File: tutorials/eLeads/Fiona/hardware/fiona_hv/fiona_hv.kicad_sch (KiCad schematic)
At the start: 63 parts, among them J101 MicroFit_VT_4, J102 MicroFit_VT_4, K1 G5Q-1A4-DC5, Q2 SSM3K333R, SW101 SW_SPDT, SW102 SW_SPDT, U101 OpAmp, U102 ATMEGA16M1, U103 OpAmp, U104 LM397, U105 MCP2561-E_SN, U106 AD8494, U107 OpAmp, Y101 Crystal_16MHz_18pF

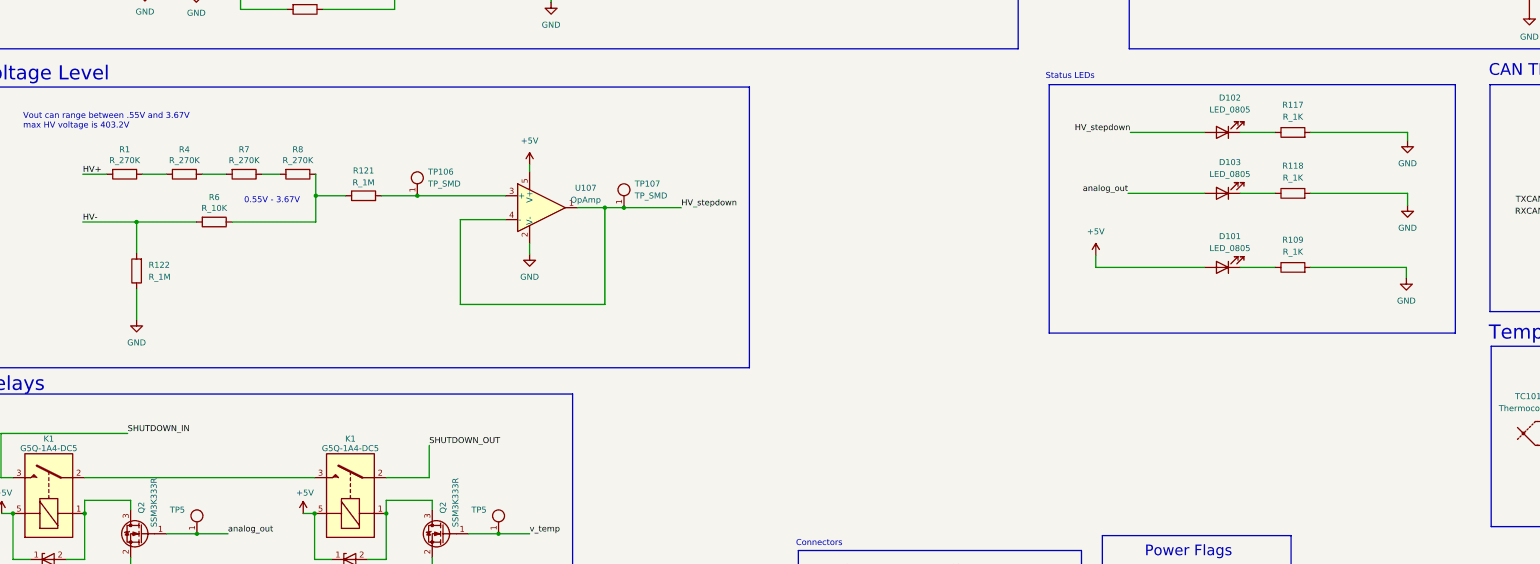
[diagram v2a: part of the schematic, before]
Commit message: Add shutdown LEDs
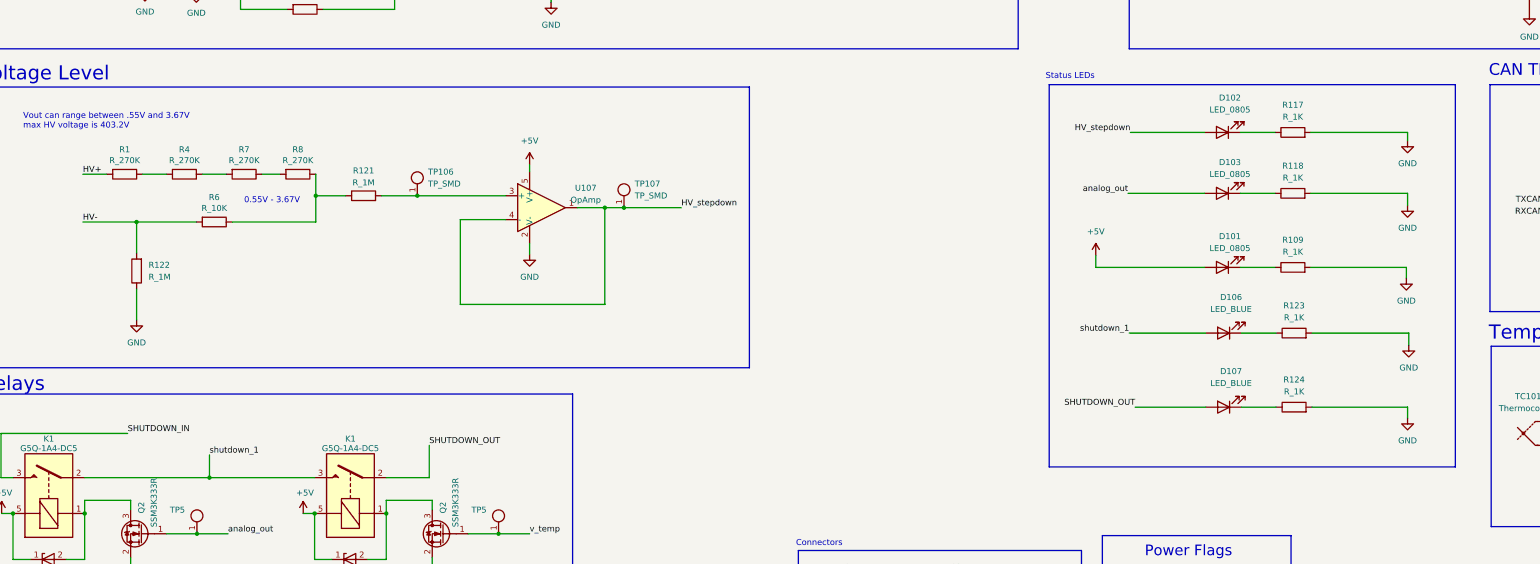
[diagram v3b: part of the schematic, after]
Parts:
- added D106, D107: LED_BLUE, OEM:CHIPLED_0805, symbol OEM:LED_BLUE
- added R123, R124: R_1K, OEM:R_0603, symbol formula:R_1K
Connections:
- net GND: now also R123.2, R124.2
- net SHUTDOWN_OUT: now also D107.2 (A)
- net shutdown_1: now reaches K1.2, K1.3
- net shutdown_1: now also D106.2 (A)
- new net: D106.1 (K), R123.1
- new net: D107.1 (K), R124.1
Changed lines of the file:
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@@
   (junction (at 102.87 41.91) (diameter 0) (color 0 0 0 0)
   )
+  (junction (at 63.754 235.966) (diameter 0) (color 0 0 0 0)
+  )
   (junction (at 277.114 54.61) (diameter 0) (color 0 0 0 0)
   )
@@
     (stroke (width 0) (type default))
   )
+  (wire (pts (xy 283.21 220.98) (xy 290.576 220.98))
+    (stroke (width 0) (type default))
+  )
   (wire (pts (xy 162.814 41.91) (xy 162.814 73.406))
     (stroke (width 0) (type default))
@@
     (stroke (width 0) (type default))
   )
+  (wire (pts (xy 275.59 205.232) (xy 259.334 205.232))
+    (stroke (width 0) (type default))
+  )
   (wire (pts (xy 371.856 215.9) (xy 371.856 218.948))
     (stroke (width 0) (type default))
@@
     (stroke (width 0) (type default))
   )
+  (wire (pts (xy 298.196 205.232) (xy 318.77 205.232))
+    (stroke (width 0) (type default))
+  )
   (wire (pts (xy 46.99 240.792) (xy 46.99 242.824))
     (stroke (width 0) (type default))
@@
     (stroke (width 0) (type default))
   )
+  (wire (pts (xy 63.754 231.14) (xy 63.754 235.966))
+    (stroke (width 0) (type default))
+  )
   (wire (pts (xy 377.952 180.34) (xy 381.762 180.34))
     (stroke (width 0) (type default))
@@
     (stroke (width 0) (type default))
   )
+  (wire (pts (xy 63.754 235.966) (xy 86.106 235.966))
+    (stroke (width 0) (type default))
+  )
   (wire (pts (xy 102.87 60.452) (xy 102.87 69.85))
     (stroke (width 0) (type default))
@@
     (stroke (width 0) (type default))
   )
+  (wire (pts (xy 298.196 220.98) (xy 318.516 220.98))
+    (stroke (width 0) (type default))
+  )
   (wire (pts (xy 362.204 118.11) (xy 362.204 125.73))
     (stroke (width 0) (type default))
   )
+  (wire (pts (xy 283.21 205.232) (xy 290.576 205.232))
+    (stroke (width 0) (type default))
+  )
   (wire (pts (xy 49.784 36.83) (xy 49.784 26.162))
     (stroke (width 0) (type default))
   )
+  (wire (pts (xy 318.516 220.98) (xy 318.516 223.266))
+    (stroke (width 0) (type default))
+  )
   (wire (pts (xy 102.87 52.832) (xy 102.87 41.91))
     (stroke (width 0) (type default))
@@
     (stroke (width 0) (type default))
   )
+  (wire (pts (xy 260.604 220.98) (xy 275.59 220.98))
+    (stroke (width 0) (type default))
+  )
   (wire (pts (xy 78.994 44.45) (xy 70.104 44.45))
     (stroke (width 0) (type default))
@@
     (stroke (width 0) (type default))
   )
+  (wire (pts (xy 318.77 205.232) (xy 318.77 207.772))
+    (stroke (width 0) (type default))
+  )
   (wire (pts (xy 365.252 167.64) (xy 369.062 167.64))
     (stroke (width 0) (type default))
@@
     (stroke (width 0) (type default))
   )
-  (wire (pts (xy 37.211 235.966) (xy 86.106 235.966))
+  (wire (pts (xy 37.211 235.966) (xy 63.754 235.966))
     (stroke (width 0) (type default))
   )
@@
     (fill (type none))
   )
-  (rectangle (start 242.316 152.4) (end 328.676 205.232)
+  (rectangle (start 242.316 152.4) (end 328.676 233.68)
     (stroke (width 0) (type default))
     (fill (type none))
@@
     (effects (font (size 1.27 1.27)) (justify left bottom))
   )
+  (label "shutdown_1" (at 63.754 231.14 0) (fields_autoplaced)
+    (effects (font (size 1.27 1.27)) (justify left bottom))
+  )
   (label "HV+" (at 36.83 171.45 0) (fields_autoplaced)
     (effects (font (size 1.27 1.27)) (justify left bottom))
   )
+  (label "shutdown_1" (at 259.334 205.232 180) (fields_autoplaced)
+    (effects (font (size 1.27 1.27)) (justify right bottom))
+  )
   (label "HV_stepdown" (at 354.584 80.01 0) (fields_autoplaced)
     (effects (font (size 1.27 1.27)) (justify left bottom))
@@
     (effects (font (size 1.27 1.27)) (justify left bottom))
   )
+  (label "SHUTDOWN_OUT" (at 260.604 220.98 180) (fields_autoplaced)
+    (effects (font (size 1.27 1.27)) (justify right bottom))
+  )
   (label "CAN-" (at 209.296 273.558 0) (fields_autoplaced)
     (effects (font (size 1.27 1.27)) (justify left bottom))
@@
     )
   )
+  (symbol (lib_id "power:GND") (at 318.77 207.772 0) (unit 1)
+    (in_bom yes) (on_board yes) (dnp no) (fields_autoplaced)
+    (property "Reference" "#PWR0145" (at 318.77 214.122 0)
+      (effects (font (size 1.27 1.27)) hide)
+    )
+    (property "Value" "GND" (at 318.77 212.598 0)
+      (effects (font (size 1.27 1.27)))
+    )
+    (property "Footprint" "" (at 318.77 207.772 0)
+      (effects (font (size 1.27 1.27)) hide)
+    )
+    (property "Datasheet" "" (at 318.77 207.772 0)
+      (effects (font (size 1.27 1.27)) hide)
+    )
+    (pin "1")
+    (instances
+      (project "fiona_hv"
+        (path "/b34db13a-c7e3-48a0-b77f-45da96e8fa7a"
+          (reference "#PWR0145") (unit 1)
+        )
+      )
+    )
+  )
   (symbol (lib_id "OEM:G5Q-1A4-DC5") (at 29.591 238.506 90) (unit 1)
     (in_bom yes) (on_board yes) (dnp no)
@@
     )
   )
+  (symbol (lib_id "power:GND") (at 318.516 223.266 0) (unit 1)
+    (in_bom yes) (on_board yes) (dnp no) (fields_autoplaced)
+    (property "Reference" "#PWR0144" (at 318.516 229.616 0)
+      (effects (font (size 1.27 1.27)) hide)
+    )
+    (property "Value" "GND" (at 318.516 228.092 0)
+      (effects (font (size 1.27 1.27)))
+    )
+    (property "Footprint" "" (at 318.516 223.266 0)
+      (effects (font (size 1.27 1.27)) hide)
+    )
+    (property "Datasheet" "" (at 318.516 223.266 0)
+      (effects (font (size 1.27 1.27)) hide)
+    )
+    (pin "1")
+    (instances
+      (project "fiona_hv"
+        (path "/b34db13a-c7e3-48a0-b77f-45da96e8fa7a"
+          (reference "#PWR0144") (unit 1)
+        )
+      )
+    )
+  )
   (symbol (lib_id "power:GND") (at 46.99 261.874 0) (mirror y) (unit 1)
     (in_bom yes) (on_board yes) (dnp no)
@@
     )
   )
+  (symbol (lib_id "formula:R_1K") (at 294.386 205.232 90) (unit 1)
+    (in_bom yes) (on_board yes) (dnp no) (fields_autoplaced)
+    (property "Reference" "R123" (at 294.386 199.39 90)
+      (effects (font (size 1.27 1.27)))
+    )
+    (property "Value" "R_1K" (at 294.386 201.93 90)
+      (effects (font (size 1.27 1.27)))
+    )
+    (property "Footprint" "OEM:R_0603" (at 294.386 207.01 0)
+      (effects (font (size 1.27 1.27)) hide)
+    )
+    (property "Datasheet" "https://www.seielect.com/Catalog/SEI-rncp.pdf" (at 294.386 203.2 0)
+      (effects (font (size 1.27 1.27)) hide)
+    )
+    (property "MFN" "DK" (at 294.386 205.232 0)
+      (effects (font (size 1.524 1.524)) hide)
+    )
+    (property "MPN" "RNCP0805FTD1K00CT-ND" (at 294.386 205.232 0)
+      (effects (font (size 1.524 1.524)) hide)
+    )
+    (property "PurchasingLink" "https://www.digikey.com/products/en?keywords=RNCP0805FTD1K00CT-ND" (at 284.226 193.04 0)
+      (effects (font (size 1.524 1.524)) hide)
+    )
+    (pin "1")
+    (pin "2")
+    (instances
+      (project "fiona_hv"
+        (path "/b34db13a-c7e3-48a0-b77f-45da96e8fa7a"
+          (reference "R123") (unit 1)
+        )
+      )
+    )
+  )
   (symbol (lib_id "formula:R_1M") (at 48.26 192.024 180) (unit 1)
     (in_bom yes) (on_board yes) (dnp no) (fields_autoplaced)
@@
     )
   )
+  (symbol (lib_id "OEM:LED_BLUE") (at 279.4 220.98 180) (unit 1)
+    (in_bom yes) (on_board yes) (dnp no) (fields_autoplaced)
+    (property "Reference" "D107" (at 280.9875 213.36 0)
+      (effects (font (size 1.27 1.27)))
+    )
+    (property "Value" "LED_BLUE" (at 280.9875 215.9 0)
+      (effects (font (size 1.27 1.27)))
+    )
+    (property "Footprint" "OEM:CHIPLED_0805" (at 279.4 220.98 0)
+      (effects (font (size 1.27 1.27)) hide)
+    )
+    (property "Datasheet" "~" (at 279.4 220.98 0)
+      (effects (font (size 1.27 1.27)) hide)
+    )
+    (pin "1")
+    (pin "2")
+    (instances
+      (project "fiona_hv"
+        (path "/b34db13a-c7e3-48a0-b77f-45da96e8fa7a"
+          (reference "D107") (unit 1)
+        )
+      )
+    )
+  )
   (symbol (lib_id "formula:R_1K") (at 102.87 56.642 180) (unit 1)
     (in_bom yes) (on_board yes) (dnp no) (fields_autoplaced)
@@
     )
   )
+  (symbol (lib_id "OEM:LED_BLUE") (at 279.4 205.232 180) (unit 1)
+    (in_bom yes) (on_board yes) (dnp no) (fields_autoplaced)
+    (property "Reference" "D106" (at 280.9875 197.612 0)
+      (effects (font (size 1.27 1.27)))
+    )
+    (property "Value" "LED_BLUE" (at 280.9875 200.152 0)
+      (effects (font (size 1.27 1.27)))
+    )
+    (property "Footprint" "OEM:CHIPLED_0805" (at 279.4 205.232 0)
+      (effects (font (size 1.27 1.27)) hide)
+    )
+    (property "Datasheet" "~" (at 279.4 205.232 0)
+      (effects (font (size 1.27 1.27)) hide)
+    )
+    (pin "1")
+    (pin "2")
+    (instances
+      (project "fiona_hv"
+        (path "/b34db13a-c7e3-48a0-b77f-45da96e8fa7a"
+          (reference "D106") (unit 1)
+        )
+      )
+    )
+  )
   (symbol (lib_id "OEM:OpAmp") (at 86.614 41.91 0) (unit 1)
     (in_bom yes) (on_board yes) (dnp no) (fields_autoplaced)
@@
         )
       )
+    )
+  )
+  (symbol (lib_id "formula:R_1K") (at 294.386 220.98 90) (unit 1)
+    (in_bom yes) (on_board yes) (dnp no) (fields_autoplaced)
+    (property "Reference" "R124" (at 294.386 215.138 90)
+      (effects (font (size 1.27 1.27)))
+    )
+    (property "Value" "R_1K" (at 294.386 217.678 90)
+      (effects (font (size 1.27 1.27)))
+    )
+    (property "Footprint" "OEM:R_0603" (at 294.386 222.758 0)
+      (effects (font (size 1.27 1.27)) hide)
+    )
+    (property "Datasheet" "https://www.seielect.com/Catalog/SEI-rncp.pdf" (at 294.386 218.948 0)
+      (effects (font (size 1.27 1.27)) hide)
+    )
+    (property "MFN" "DK" (at 294.386 220.98 0)
+      (effects (font (size 1.524 1.524)) hide)
+    )
+    (property "MPN" "RNCP0805FTD1K00CT-ND" (at 294.386 220.98 0)
+      (effects (font (size 1.524 1.524)) hide)
+    )
+    (property "PurchasingLink" "https://www.digikey.com/products/en?keywords=RNCP0805FTD1K00CT-ND" (at 284.226 208.788 0)
+      (effects (font (size 1.524 1.524)) hide)
+    )
+    (pin "1")
+    (pin "2")
+    (instances
+      (project "fiona_hv"
+        (path "/b34db13a-c7e3-48a0-b77f-45da96e8fa7a"
+          (reference "R124") (unit 1)
+        )
+      )

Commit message: Crying screaming pcb
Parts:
- added J1: CONN_02X03, footprints:Pin_Header_Straight_2x03, symbol formula:CONN_02X03
- added J104: MicroFit_RA_V_2, footprints:MicroFit_RA_V_2, symbol formula:MicroFit_RA_V_2
- added TP111: TP_SMD, footprints:Test_Point_SMD, symbol formula:TP_SMD
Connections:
- net +5 is gone; now on net +5V: J101.1
- net +5V: now also J1.2 (P2)
- net GND: now also J1.6 (P6), TP111.1
- net HV+: now also J104.1
- net HV-: now also J104.2
- net at R101.2, RV101.1: no longer SW101.1 (A)
- net MISO: now reaches U102.1 ((PCINT18/PSCIN2/OC1A/MISO_A)PD2)
- net MISO: now also J1.1 (P1)
- net SCK: now reaches U102.12 ((PCINT20/ADC1/RXD/RXLIN/ICP1A/SCK_A)PD4)
- net SCK: now also J1.3 (P3)
- net MOSI: now reaches U102.2 ((PCINT19/TXD/TXLIN/OC0A/~{SS}/MOSI_A)PD3)
- net MOSI: now also J1.4 (P4)
- net at R104.2, RV102.1: no longer SW102.1 (A)
- net at RV101.2: now also SW101.1 (A)
- net at RV102.2: now also SW102.1 (A)
- new net RESET: J1.5 (P5)
- no-connect marks 23 -> 20
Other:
- note added: "16M1 PROGRAMMING HEADER"
- note added: "GND Testpoint"
- moved on the sheet: J101, J102

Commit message: oof board
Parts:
- removed C105, C106: C_22pF, symbol Device:C
- removed SW101, SW102: SW_SPDT, symbol Switch:SW_SPDT
- removed TP5 (x2): BSPD, footprints:Test_Point_SMD, symbol OEM:TP_SMD
- added C105, C108: C_30pF, footprints:C_0805_OEM, symbol formula:C_30pF
- added SW101, SW102, SW103, SW104: SW_DIP_x01, Button_Switch_SMD:SW_DIP_SPSTx01_Slide_9.78x4.72mm_W8.61mm_P2.54mm, symbol Switch:SW_DIP_x01
- RV101, RV102: footprint (none) -> footprints:Potentiometer_Trimmer_Bourns_TCC3
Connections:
- net CAN_H is gone; now on net CAN+: R111.1, U105.7 (CANH)
- net CAN_L is gone; now on net CAN-: R111.2, U105.6 (CANL)
- net A: now also SW101.1
- net B: now also SW102.1
- net GND: now also C105.2, C108.2
- net at U103.3 (+): now also SW102.2, SW104.2
- net at U102.11 ((PCINT26/ADC0/XTAL2)PE2), Y101.1: now also C108.1
- net at U102.10 ((PCINT25/OC0B/XTAL1)PE1), Y101.3: now also C105.1
- net at RV102.2: now also SW104.1
- net at RV101.2: now also SW103.1
- net at U101.3 (+): now also SW101.2, SW103.2
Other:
- moved on the sheet: R119, RV101
